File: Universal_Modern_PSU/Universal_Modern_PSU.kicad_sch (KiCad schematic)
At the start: 16 parts, among them J1 +12VDC Input, J2 Power Output, Q1 SUP53P06-20-E3, U1 DFR0831, U2 NKE1212SC, U3 R-78CK5.0-0.5

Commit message: Minor updates
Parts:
- C2, C3, C4: footprint Capacitor_THT:C_Radial_D5.0mm_H5.0mm_P2.00mm -> Capacitor_THT:C_Radial_D6.3mm_H7.0mm_P2.50mm

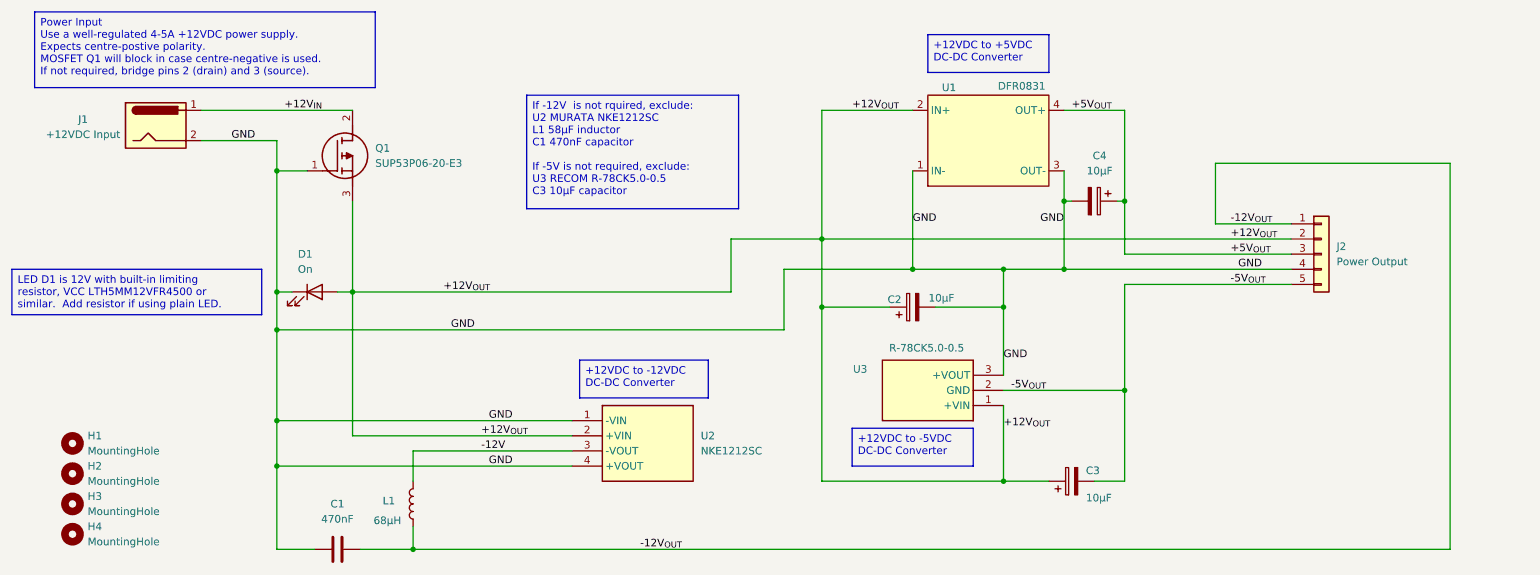
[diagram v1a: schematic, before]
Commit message: Added additional capacitors
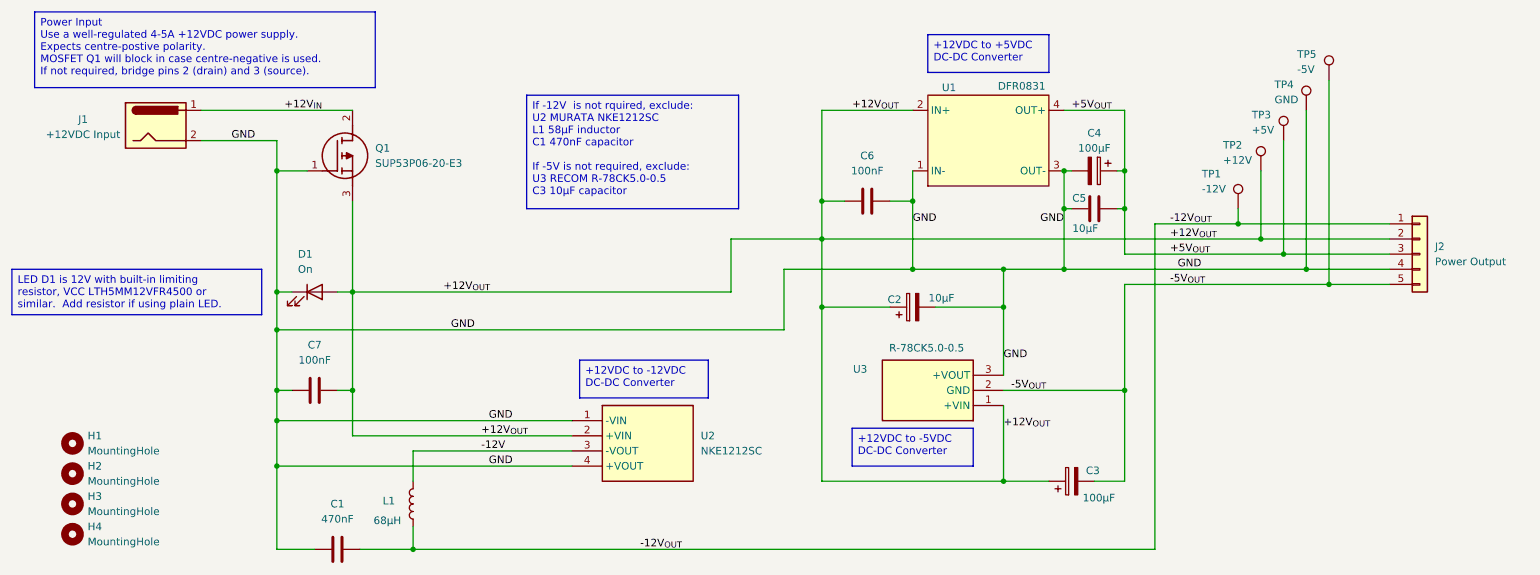
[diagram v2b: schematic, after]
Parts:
- added C5: 10µF, Capacitor_THT:C_Disc_D5.0mm_W2.5mm_P5.00mm, symbol Device:C
- added C6, C7: 100nF, Capacitor_THT:C_Disc_D5.0mm_W2.5mm_P5.00mm, symbol Device:C
- added TP1: -12V, TestPoint:TestPoint_Pad_D2.5mm, symbol Connector:TestPoint
- added TP2: +12V, TestPoint:TestPoint_Pad_D2.5mm, symbol Connector:TestPoint
- added TP3: +5V, TestPoint:TestPoint_Pad_D2.5mm, symbol Connector:TestPoint
- added TP4: GND, TestPoint:TestPoint_Pad_D2.5mm, symbol Connector:TestPoint
- added TP5: -5V, TestPoint:TestPoint_Pad_D2.5mm, symbol Connector:TestPoint
- C3, C4: value 10µF -> 100µF; footprint Capacitor_THT:C_Radial_D6.3mm_H7.0mm_P2.50mm -> Capacitor_THT:CP_Radial_D8.0mm_P5.00mm
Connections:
- net +12V_{OUT}: now also C6.1, C7.2, TP2.1
- net +5V_{OUT}: now also C5.2, TP3.1
- net -12V_{OUT}: now also TP1.1
- net -5V_{OUT}: now also TP5.1
- net GND: now also C5.1, C6.2, C7.1, TP4.1
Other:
- moved on the sheet: C4, J2
